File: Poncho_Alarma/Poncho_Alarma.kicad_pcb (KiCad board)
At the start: 2 copper layers, 5 parts, among them Q1 2N7002, Q2 2N7002

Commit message: arreglado lo de la libreria
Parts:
- added D1: LED_Rojo, LED_THT:LED_D3.0mm, F.Cu at (239.9, 219.8)
- added D2: LED_Rojo, LED_THT:LED_D3.0mm, F.Cu at (214.3, 232.2)
- added D5: LED_Rojo, LED_THT:LED_D3.0mm, F.Cu at (488.6, 73.9)
- added D6: LED_Rojo, LED_THT:LED_D3.0mm, F.Cu at (488.6, 78.4)
- added D7: LED_Rojo, LED_THT:LED_D3.0mm, F.Cu at (481.6, 86.5)
- added D8: LED_Rojo, LED_THT:LED_D3.0mm, F.Cu at (481.6, 81.9)
- added J1: ESP8266, Connector_PinHeader_2.54mm:PinHeader_2x04_P2.54mm_Vertical, F.Cu at (279.6, 106.0)
- added J2: Salidas, TerminalBlock:TerminalBlock_bornier-6_P5.08mm, F.Cu at (194.5, 221.6)
- added J3: Entradas, TerminalBlock:TerminalBlock_bornier-4_P5.08mm, F.Cu at (469.1, 71.3)
- added K1: RELAY_C, Poncho-PLC:Relay_C, F.Cu at (230.7, 227.8)
- added K2: RELAY_C, Poncho-PLC:Relay_C, F.Cu at (199.8, 235.8)
- added R1: 10K, Resistor_THT:R_Axial_DIN0204_L3.6mm_D1.6mm_P5.08mm_Horizontal, F.Cu at (192.7, 205.6)
- added R10: 4.7K, Resistor_THT:R_Axial_DIN0204_L3.6mm_D1.6mm_P5.08mm_Horizontal, F.Cu at (474.3, 87.2)
- added R11: 4.7K, Resistor_THT:R_Axial_DIN0204_L3.6mm_D1.6mm_P5.08mm_Horizontal, F.Cu at (467.3, 82.9)
- added R12: 4.7K, Resistor_THT:R_Axial_DIN0204_L3.6mm_D1.6mm_P5.08mm_Horizontal, F.Cu at (488.1, 70.5)
- added R13: 4.7K, Resistor_THT:R_Axial_DIN0204_L3.6mm_D1.6mm_P5.08mm_Horizontal, F.Cu at (474.3, 78.6)
- added R14: 2.2K, Resistor_THT:R_Axial_DIN0204_L3.6mm_D1.6mm_P5.08mm_Horizontal, F.Cu at (467.3, 85.0)
- added R15: 100K, Resistor_THT:R_Axial_DIN0204_L3.6mm_D1.6mm_P5.08mm_Horizontal, F.Cu at (474.3, 80.7)
- added R16: 2.2K, Resistor_THT:R_Axial_DIN0204_L3.6mm_D1.6mm_P5.08mm_Horizontal, F.Cu at (467.3, 87.2)
- added R17: 100K, Resistor_THT:R_Axial_DIN0204_L3.6mm_D1.6mm_P5.08mm_Horizontal, F.Cu at (481.4, 76.4)
- added R18: 2.2K, Resistor_THT:R_Axial_DIN0204_L3.6mm_D1.6mm_P5.08mm_Horizontal, F.Cu at (474.3, 82.9)
- added R19: 100K, Resistor_THT:R_Axial_DIN0204_L3.6mm_D1.6mm_P5.08mm_Horizontal, F.Cu at (474.3, 85.0)
- added R2: 100k, Resistor_THT:R_Axial_DIN0204_L3.6mm_D1.6mm_P5.08mm_Horizontal, F.Cu at (215.8, 226.7)
- added R20: 2.2K, Resistor_THT:R_Axial_DIN0204_L3.6mm_D1.6mm_P5.08mm_Horizontal, F.Cu at (481.4, 78.6)
- added R21: 100K, Resistor_THT:R_Axial_DIN0204_L3.6mm_D1.6mm_P5.08mm_Horizontal, F.Cu at (467.3, 76.4)
- added R3: 100k, Resistor_THT:R_Axial_DIN0204_L3.6mm_D1.6mm_P5.08mm_Horizontal, F.Cu at (208.7, 238.6)
- added R4: 330, Resistor_THT:R_Axial_DIN0204_L3.6mm_D1.6mm_P5.08mm_Horizontal, F.Cu at (208.7, 226.7)
- added R5: 330, Resistor_THT:R_Axial_DIN0204_L3.6mm_D1.6mm_P5.08mm_Horizontal, F.Cu at (208.7, 228.8)
- added R6: R_Small3.3K, Resistor_THT:R_Axial_DIN0204_L3.6mm_D1.6mm_P5.08mm_Horizontal, F.Cu at (467.3, 78.6)
- added R7: R_Small3.3K, Resistor_THT:R_Axial_DIN0204_L3.6mm_D1.6mm_P5.08mm_Horizontal, F.Cu at (488.1, 68.4)
- added R8: R_Small3.3K, Resistor_THT:R_Axial_DIN0204_L3.6mm_D1.6mm_P5.08mm_Horizontal, F.Cu at (474.3, 76.4)
- added R9: R_Small3.3K, Resistor_THT:R_Axial_DIN0204_L3.6mm_D1.6mm_P5.08mm_Horizontal, F.Cu at (467.3, 80.7)
- added U1: TLP627-4, Package_DIP:DIP-16_W7.62mm, F.Cu at (457.6, 68.9)
- added XA1: Conn_Poncho2P_2x_20x2, Poncho-PLC:poncho_grande, F.Cu at (269.6, 130.8)
- moved Q1 121.3 mm to (216.5, 236.2)
- moved D3 117.2 mm to (210.4, 231.0)
- moved D4 117.2 mm to (210.4, 233.3)
- moved Q2 114.8 mm to (219.7, 229.5)
- moved DS1 91.3 mm to (286.0, 70.4)

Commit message: Posicionado terminado
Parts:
- R1: footprint Resistor_THT:R_Axial_DIN0204_L3.6mm_D1.6mm_P5.08mm_Horizontal -> Poncho-PLC:TRIMER_V
- moved R12 354.7 mm to (133.3, 69.8)
- moved R10 350.3 mm to (124.5, 69.8)
- moved R7 345.9 mm to (142.2, 73.7)
- moved R6 342.9 mm to (124.5, 73.7)
- moved R8 341.0 mm to (133.3, 73.7)
- moved R11 325.3 mm to (142.2, 69.8)
- moved R13 323.3 mm to (151.1, 73.7)
- moved U1 321.8 mm to (135.9, 64.8), turned to 90 degrees
- moved R20 318.3 mm to (163.8, 57.1)
- moved R17 317.5 mm to (163.8, 76.2)
- moved D5 316.8 mm to (172.7, 49.5)
- moved R9 316.4 mm to (151.1, 69.8)
- moved D6 315.9 mm to (172.7, 72.4)
- moved R15 311.8 mm to (163.8, 52.1)
- moved R18 311.0 mm to (163.8, 64.8)
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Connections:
- J2 pad 1: Net-(J2-Pad1) -> /Salidas/K1_NA
- J2 pad 2: Net-(J2-Pad2) -> /Salidas/K1_C
- J2 pad 3: Net-(J2-Pad3) -> /Salidas/K1_NC
- J2 pad 4: Net-(J2-Pad4) -> /Salidas/K2_NA
- J2 pad 5: Net-(J2-Pad5) -> /Salidas/K2_C
- J2 pad 6: Net-(J2-Pad6) -> /Salidas/K2_NC
- K1 pad 1: Net-(J2-Pad3) -> /Salidas/K1_C
- K1 pad 3: Net-(J2-Pad2) -> /Salidas/K1_NA
- K1 pad 4: Net-(J2-Pad1) -> /Salidas/K1_NC
- K2 pad 1: Net-(J2-Pad6) -> /Salidas/K2_C
- K2 pad 3: Net-(J2-Pad5) -> /Salidas/K2_NA
- K2 pad 4: Net-(J2-Pad4) -> /Salidas/K2_NC
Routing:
- net /Salidas/K2_C: track 0.00 -> 43.9 mm
- net /Salidas/K1_C: track 0.00 -> 41.7 mm
- net /Salidas/K2_NC: track 0.00 -> 30.1 mm
- net /Salidas/K1_NC: track 0.00 -> 29.0 mm
- net /Salidas/K2_NA: track 0.00 -> 28.2 mm
- net Net-(D3-Pad2): track 0.00 -> 27.7 mm
- net Net-(D4-Pad2): track 0.00 -> 27.3 mm
- net /Salidas/K1_NA: track 0.00 -> 27.1 mm
- net +5V: track 0.00 -> 24.7 mm
- net GND: track 0.00 -> 22.8 mm
- net Net-(D2-Pad1): track 0.00 -> 12.0 mm
- net Net-(D1-Pad1): track 0.00 -> 12.0 mm
- net Net-(Q2-Pad1): track 0.00 -> 10.6 mm
- net /Salidas/Out_1: track 0.00 -> 10.6 mm
- net Net-(R10-Pad2): track 0.00 -> 8.45 mm
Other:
- net class Default: clearance 0.2 -> 0.35; trace_width 0.25 -> 0.4
- net class OUT_RELAY added: clearance 0.35, trace_width 0.8, via_dia 0.8, via_drill 0.4
- net class POWER added: clearance 0.35, trace_width 0.6, via_dia 0.8, via_drill 0.4
- rule trace_clearance: 0.2 -> 0.35

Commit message: Terminado ruteado
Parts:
- moved R11 8.89 mm to (133.3, 69.8)
- moved R12 8.89 mm to (142.2, 69.8)
- moved R7 8.89 mm to (133.3, 73.7)
- moved R8 8.89 mm to (142.2, 73.7)
- moved R13 3.81 mm to (151.1, 69.8)
- moved R9 3.81 mm to (151.1, 73.7)
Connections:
- XA1 pad 76: /Entradas/In_3 -> /Entradas/In_1
- XA1 pad 80: /Entradas/In_1 -> /Entradas/In_3
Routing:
- net GND: track 22.8 -> 221.3 mm, vias 0 -> 2
- net +5V: track 24.7 -> 196.7 mm, vias 0 -> 2
- net Net-(DS1-Pad4): track 0.00 -> 105.4 mm, vias 0 -> 1
- net Net-(DS1-Pad6): track 0.00 -> 99.4 mm
- net +3V3: track 0.00 -> 81.5 mm
- net Net-(DS1-Pad11): track 0.00 -> 80.2 mm
- net /Salidas/Out_1: track 10.6 -> 87.5 mm, vias 0 -> 1
- net Net-(DS1-Pad12): track 0.00 -> 75.5 mm
- net Net-(DS1-Pad13): track 0.00 -> 71.0 mm
- net /Entradas/In_4: track 0.00 -> 68.7 mm
- net Net-(DS1-Pad14): track 0.00 -> 64.0 mm
- net /Entradas/In_1: track 0.00 -> 62.5 mm
- net /Entradas/In_2: track 0.00 -> 56.8 mm
- net Net-(D6-Pad1): track 0.00 -> 56.5 mm
- net Net-(D5-Pad1): track 0.00 -> 52.0 mm
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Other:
- net class Default: via_dia 0.8 -> 1.5; via_drill 0.4 -> 0.7
- net class OUT_RELAY: via_dia 0.8 -> 1.5; via_drill 0.4 -> 0.7
- net class POWER: via_dia 0.8 -> 1.5; via_drill 0.4 -> 0.7

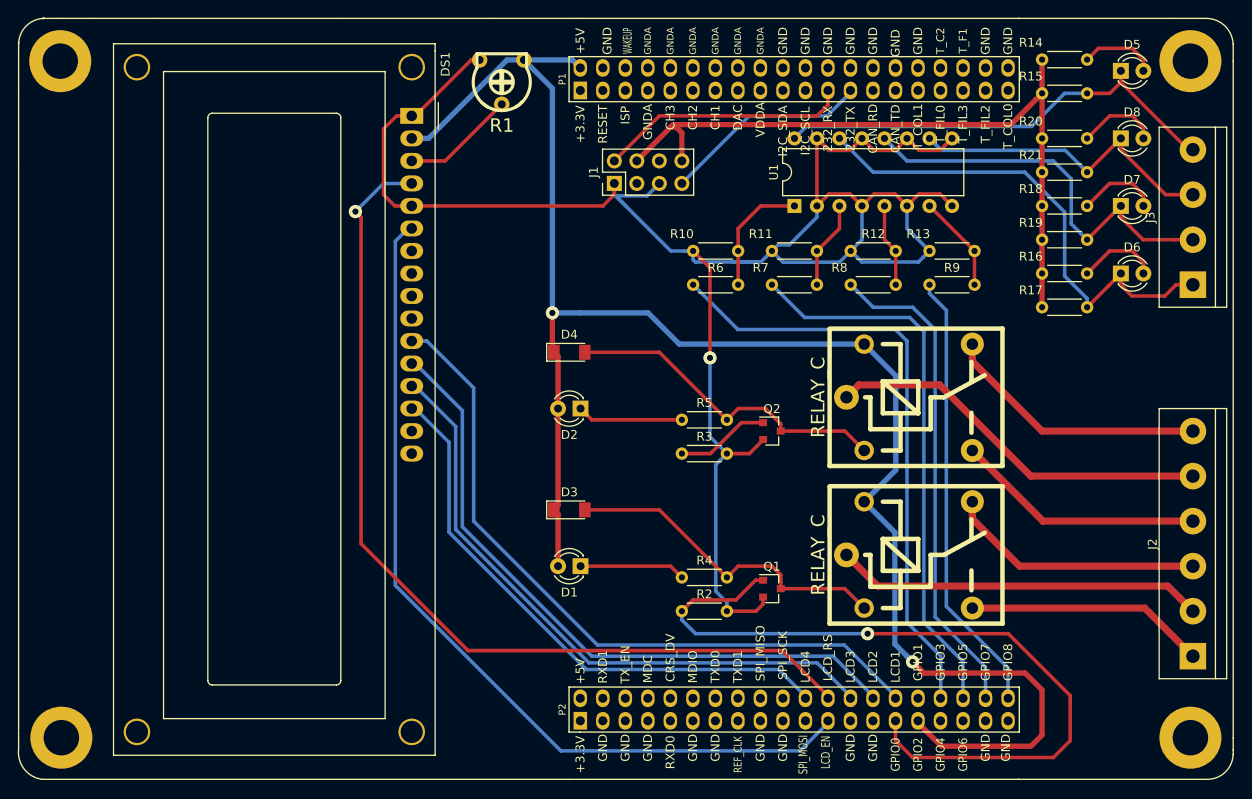
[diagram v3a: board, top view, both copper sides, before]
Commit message: mascara cobre
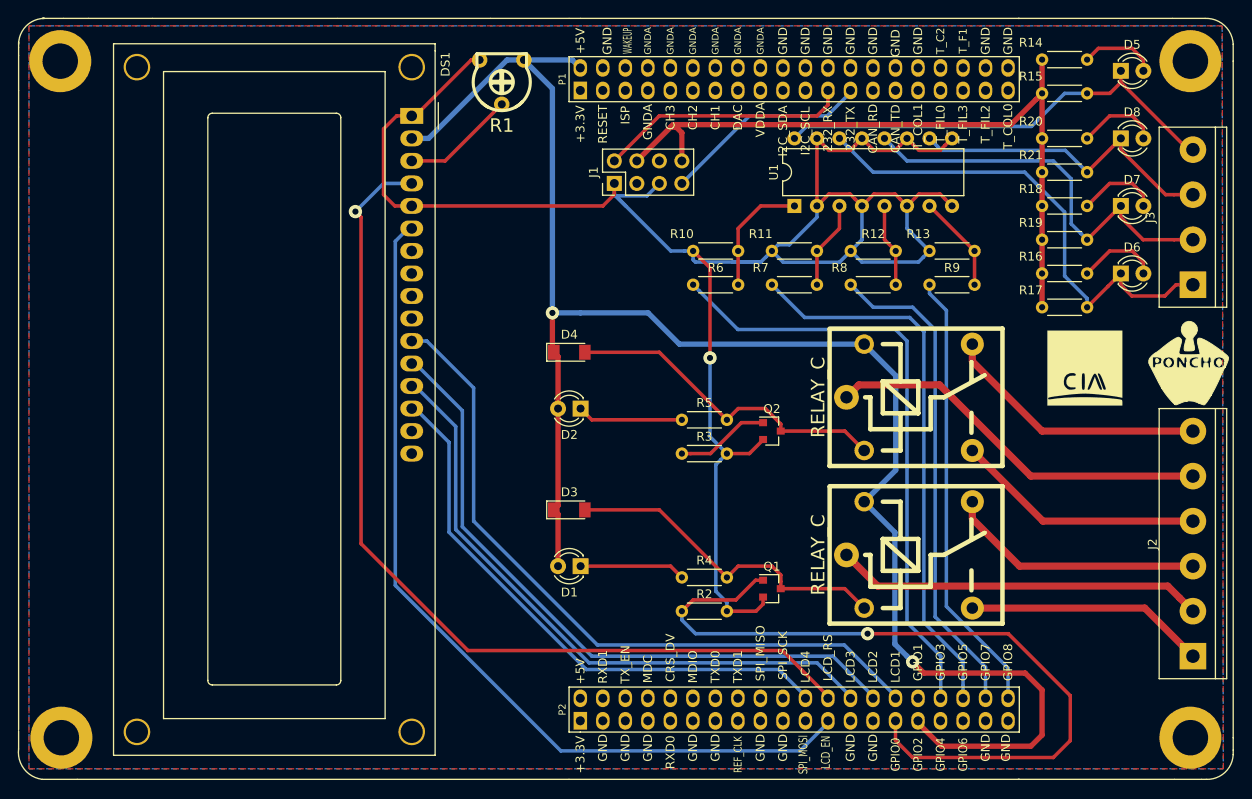
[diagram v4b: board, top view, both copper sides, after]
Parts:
- added G***: LOGO, Poncho-PLC:Logo_Poncho, F.Cu at (180.3, 82.5)
- added G102: LOGO_CIAA, Poncho-PLC:LOGO-CIAA, F.Cu at (168.7, 83.1)
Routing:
- added copper zone on B.Cu, net GND
- added copper zone on F.Cu, net GND

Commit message: Correcciónes
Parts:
- added MP1: Plantilla_EDU-CIAA, Poncho-PLC:Plantilla_EDU-CIAA, F.Cu at (240.0, 79.0)
- D3, D4: footprint Diode_SMD:D_MiniMELF -> Diode_THT:D_A-405_P7.62mm_Horizontal
- J1: footprint Connector_PinHeader_2.54mm:PinHeader_2x04_P2.54mm_Vertical -> local:ESP-01
- moved J2 154.6 mm to (29.8, 148.4), turned to 0 degrees
- moved G*** 137.1 mm to (46.0, 110.2), turned to 270 degrees
- moved J3 132.3 mm to (71.7, 148.4), turned to 0 degrees
- moved G102 123.7 mm to (46.0, 99.5), turned to 270 degrees
- moved D6 120.7 mm to (73.0, 140.3), turned to 270 degrees
- moved D7 119.1 mm to (80.6, 140.3), turned to 270 degrees
- moved D5 118.9 mm to (95.9, 140.3), turned to 270 degrees
- moved D8 118.5 mm to (88.2, 140.3), turned to 270 degrees
- moved K1 112.5 mm to (41.2, 133.3), turned to 0 degrees
- moved R17 109.6 mm to (69.2, 131.4), turned to 270 degrees
- moved R16 108.3 mm to (73.0, 131.4), turned to 270 degrees
- moved R19 107.3 mm to (76.8, 131.4), turned to 270 degrees
- moved R18 106.6 mm to (80.6, 131.4), turned to 270 degrees
- moved R14 106.6 mm to (97.1, 131.4), turned to 270 degrees
- moved R21 106.2 mm to (84.4, 131.4), turned to 270 degrees
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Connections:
- Q2 pad 1: Net-(Q2-Pad1) -> /Salidas/Out_2
- R3 pad 1: Net-(Q2-Pad1) -> /Salidas/Out_2
- XA1 pad 1: Net-(XA1-Pad1) -> +3V3
- XA1 pad 71: +5V -> /Salidas/Out_2
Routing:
- net /Salidas/Out_2: track 0.00 -> 95.6 mm, vias 0 -> 1
- net +5V: track 196.7 -> 175.9 mm
- net Net-(D4-Pad2): track 37.6 -> 57.3 mm
- net /Salidas/K2_C: track 43.9 -> 26.4 mm
- net /Salidas/K2_NC: track 30.1 -> 12.6 mm
- net /Salidas/K1_NC: track 29.0 -> 12.0 mm
- net /Salidas/K2_NA: track 28.2 -> 11.8 mm
- net /Salidas/K1_C: track 41.7 -> 25.8 mm
- net /Salidas/K1_NA: track 27.1 -> 11.3 mm
- net Net-(J1-Pad7): track 23.5 -> 38.1 mm
- net Net-(D3-Pad2): track 38.1 -> 51.7 mm
- net Net-(Q2-Pad1): track 10.6 -> 0.00 mm
- net +3V3: track 81.5 -> 91.8 mm
- net GND: track 221.3 -> 226.4 mm
- net Net-(J1-Pad2): track 28.4 -> 30.4 mm, vias 0 -> 1
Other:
- board text added: "Ind. Arg."
- board text added: "www.proyecto-ciaa.com.ar"
